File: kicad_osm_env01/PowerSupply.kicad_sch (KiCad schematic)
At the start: 27 parts, among them J5 USB_C_Receptacle_USB2.0, U1 LM66100DCKR, U4 LM66100DCKR, U9 TLV1117LV33DCYR

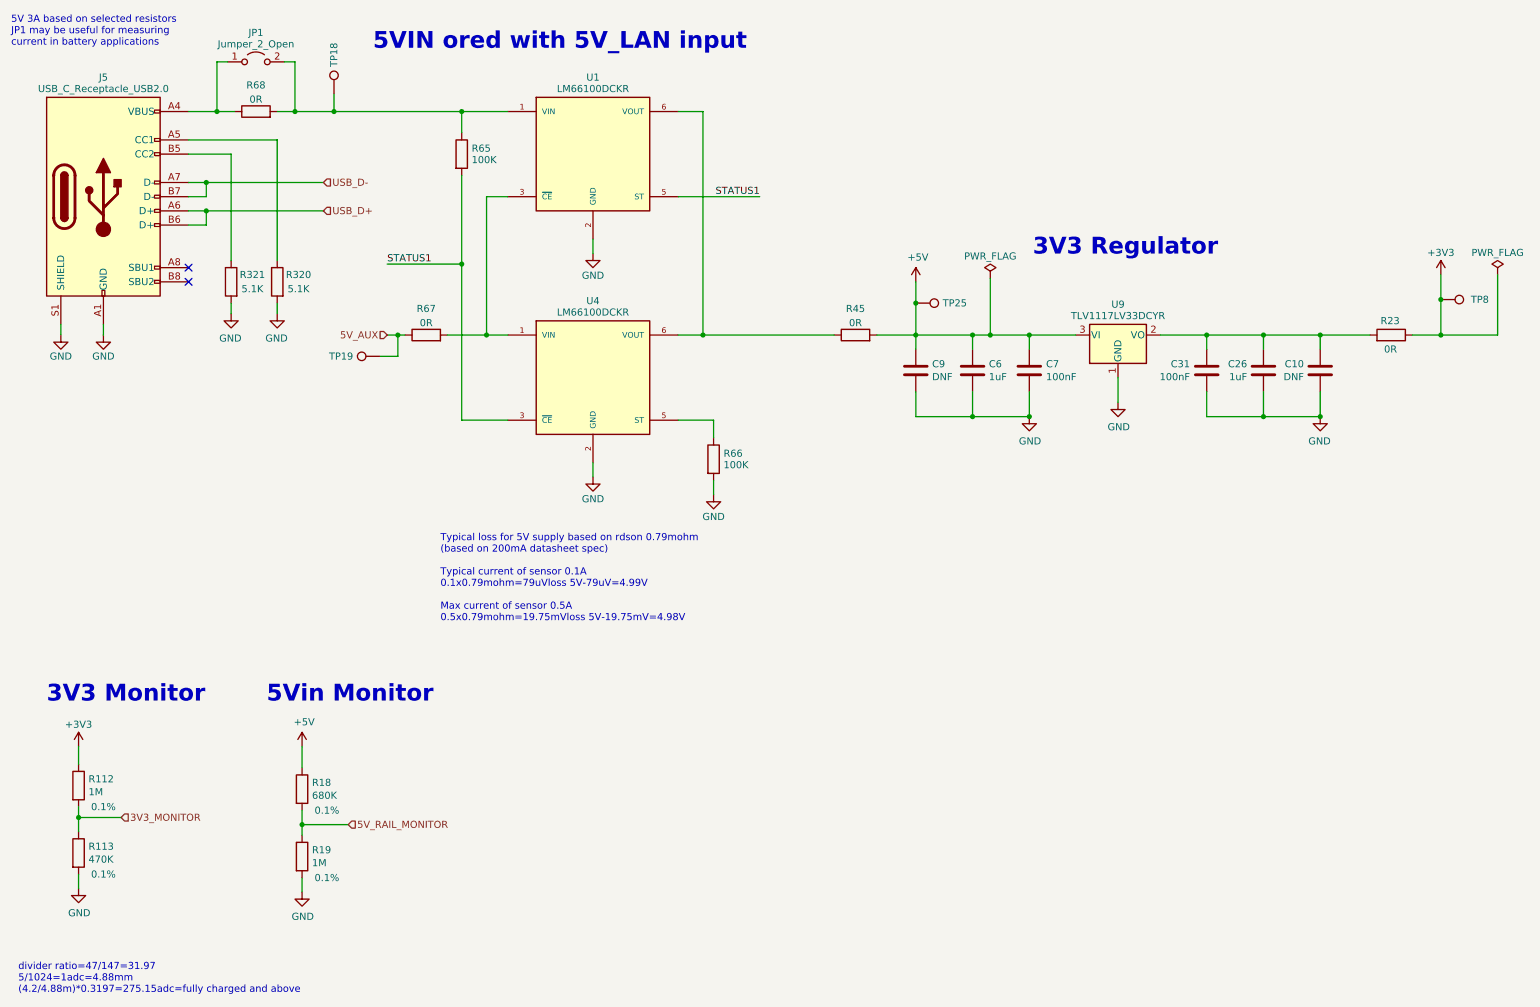
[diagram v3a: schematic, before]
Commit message: updated schematics
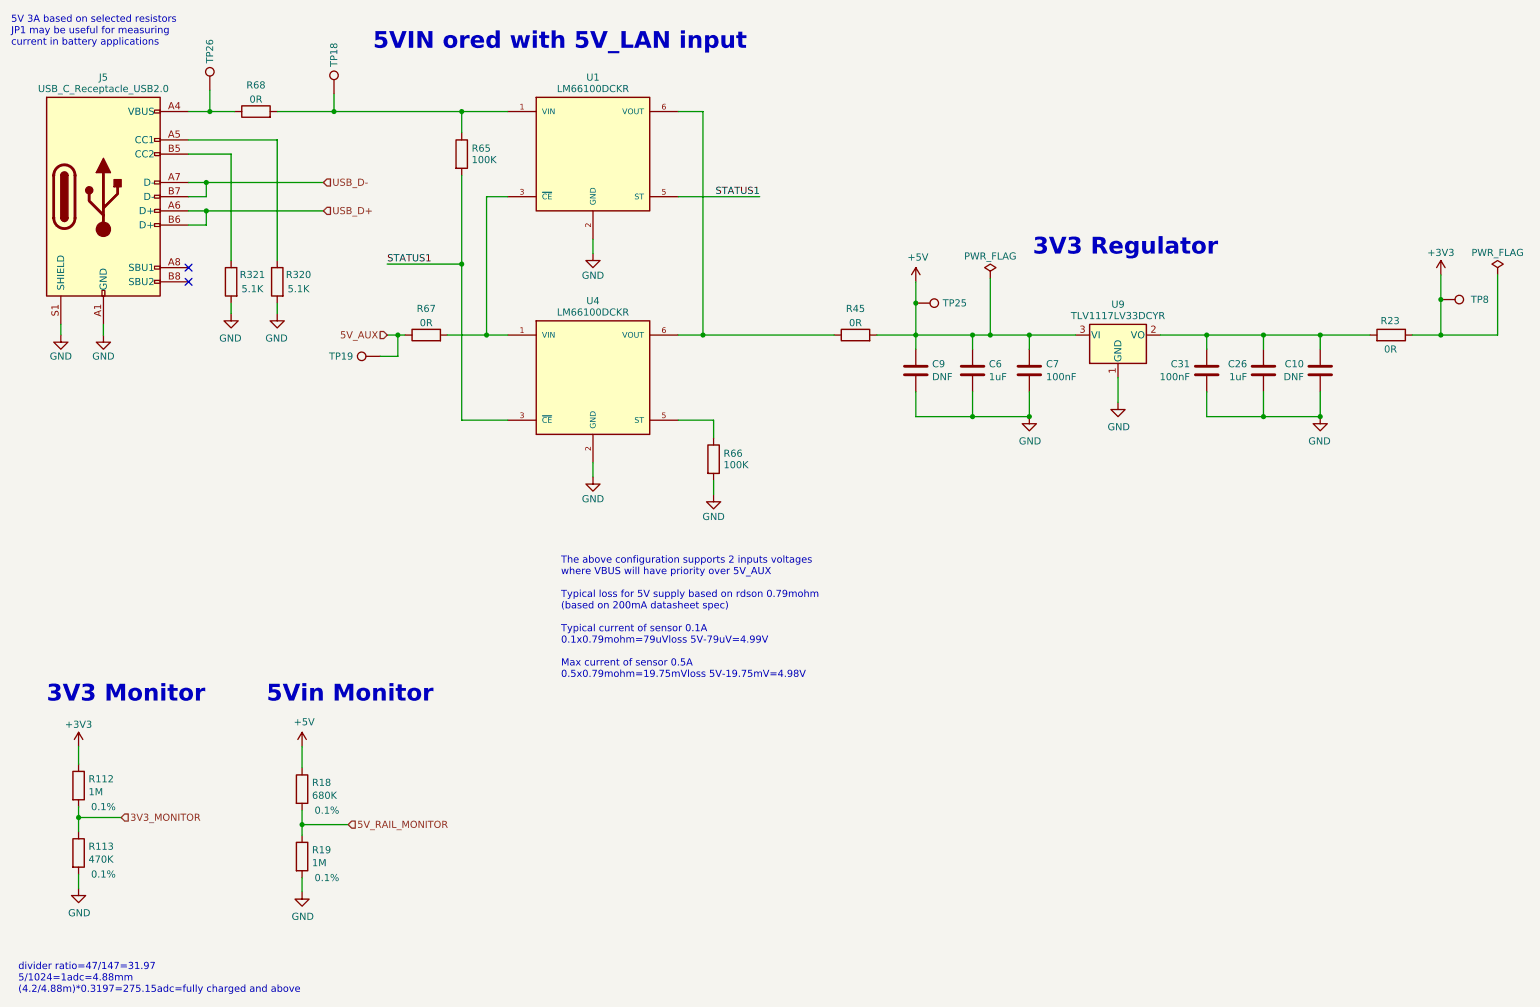
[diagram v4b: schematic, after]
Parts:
- removed JP1: Jumper_2_Open, Connector_PinSocket_2.54mm:PinSocket_1x02_P2.54mm_Vertical, symbol Jumper:Jumper_2_Open
- added TP26: Test_Point, TestPoint:TestPoint_THTPad_D1.0mm_Drill0.5mm, symbol OSM_env01-rescue:Test_Point-Connector-ESP32-EVB_Rev_D-rescue
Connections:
- net at J5.A4 (VBUS), J5.A9 (VBUS), J5.B4 (VBUS)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: now also TP26.1
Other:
- note added: "The above configuration supports 2 inputs voltages where VBUS will have priority over 5V_AUX Typical loss for 5V supply based on rdson 0.79mohm (based on 200mA datasheet spec) Typical current of sensor 0.1A 0.1x0.79mohm=79uVloss 5V-79uV=4.99V Max current of sensor 0.5A 0.5x0.79mohm=19.75mVloss 5V-19.75mV=4.98V"
- note removed: "Typical loss for 5V supply based on rdson 0.79mohm (based on 200mA datasheet spec) Typical current of sensor 0.1A 0.1x0.79mohm=79uVloss 5V-79uV=4.99V Max current of sensor 0.5A 0.5x0.79mohm=19.75mVloss 5V-19.75mV=4.98V"
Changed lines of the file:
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@@
   (junction (at 196.215 90.17) (diameter 0) (color 0 0 0 0)
   )
+  (junction (at 49.53 35.56) (diameter 0) (color 0 0 0 0)
+  )
   (junction (at 269.875 75.565) (diameter 0) (color 0 0 0 0)
   )
@@
   (junction (at 83.185 75.565) (diameter 0) (color 0 0 0 0)
   )
-  (junction (at 50.8 35.56) (diameter 0) (color 0 0 0 0)
-  )
   (junction (at 227.965 75.565) (diameter 0) (color 0 0 0 0)
   )
@@
   )
   (junction (at 137.795 75.565) (diameter 0) (color 0 0 0 0)
-  )
-  (junction (at 64.77 35.56) (diameter 0) (color 0 0 0 0)
   )
   (junction (at 175.895 75.565) (diameter 0) (color 0 0 0 0)
@@
     (stroke (width 0) (type default))
   )
-  (wire (pts (xy 50.8 35.56) (xy 53.975 35.56))
-    (stroke (width 0) (type default))
-  )
   (wire (pts (xy 219.71 75.565) (xy 227.965 75.565))
     (stroke (width 0) (type default))
@@
     (stroke (width 0) (type default))
   )
-  (wire (pts (xy 50.8 26.67) (xy 50.8 35.56))
+  (wire (pts (xy 49.53 35.56) (xy 53.975 35.56))
     (stroke (width 0) (type default))
   )
@@
     (stroke (width 0) (type default))
   )
-  (wire (pts (xy 62.865 26.67) (xy 64.77 26.67))
-    (stroke (width 0) (type default))
-  )
   (wire (pts (xy 102.87 50.8) (xy 99.06 50.8))
     (stroke (width 0) (type default))
@@
     (stroke (width 0) (type default))
   )
+  (wire (pts (xy 49.53 31.75) (xy 49.53 35.56))
+    (stroke (width 0) (type default))
+  )
   (wire (pts (xy 212.09 83.185) (xy 212.09 87.63))
     (stroke (width 0) (type default))
@@
     (stroke (width 0) (type default))
   )
-  (wire (pts (xy 61.595 35.56) (xy 64.77 35.56))
+  (wire (pts (xy 61.595 35.56) (xy 71.755 35.56))
     (stroke (width 0) (type default))
   )
@@
     (stroke (width 0) (type default))
   )
-  (wire (pts (xy 52.705 26.67) (xy 50.8 26.67))
-    (stroke (width 0) (type default))
-  )
   (wire (pts (xy 48.895 48.26) (xy 45.72 48.26))
     (stroke (width 0) (type default))
@@
     (stroke (width 0) (type default))
   )
-  (wire (pts (xy 64.77 35.56) (xy 71.755 35.56))
-    (stroke (width 0) (type default))
-  )
   (wire (pts (xy 189.23 75.565) (xy 196.215 75.565))
     (stroke (width 0) (type default))
@@
     (stroke (width 0) (type default))
   )
-  (wire (pts (xy 45.72 35.56) (xy 50.8 35.56))
+  (wire (pts (xy 45.72 35.56) (xy 49.53 35.56))
     (stroke (width 0) (type default))
   )
@@
   )
   (wire (pts (xy 26.035 149.225) (xy 26.035 152.4))
-    (stroke (width 0) (type default))
-  )
-  (wire (pts (xy 64.77 26.67) (xy 64.77 35.56))
     (stroke (width 0) (type default))
   )
@@
     (effects (font (size 2.9972 2.9972) (thickness 0.5994) bold) (justify left bottom))
   )
-  (text "Typical loss for 5V supply based on rdson 0.79mohm\n(based on 200mA datasheet spec)\n\nTypical current of sensor 0.1A\n0.1x0.79mohm=79uVloss 5V-79uV=4.99V\n\nMax current of sensor 0.5A\n0.5x0.79mohm=19.75mVloss 5V-19.75mV=4.98V"
-    (at 90.805 127 0)
+  (text "The above configuration supports 2 inputs voltages\nwhere VBUS will have priority over 5V_AUX\n\nTypical loss for 5V supply based on rdson 0.79mohm\n(based on 200mA datasheet spec)\n\nTypical current of sensor 0.1A\n0.1x0.79mohm=79uVloss 5V-79uV=4.99V\n\nMax current of sensor 0.5A\n0.5x0.79mohm=19.75mVloss 5V-19.75mV=4.98V"
+    (at 112.395 137.16 0)
     (effects (font (size 1.27 1.27)) (justify left bottom))
   )
@@
         (path "/ab8b0540-9c9f-4195-88f5-7bed0b0a8ed6/00000000-0000-0000-0000-000060688d25"
           (reference "#PWR046") (unit 1)
-        )
-      )
-    )
-  )
-  (symbol (lib_id "Jumper:Jumper_2_Open") (at 57.785 26.67 0) (unit 1)
-    (in_bom yes) (on_board yes) (dnp no) (fields_autoplaced)
-    (property "Reference" "JP1" (at 57.785 21.439 0)
-      (effects (font (size 1.27 1.27)))
-    )
-    (property "Value" "Jumper_2_Open" (at 57.785 23.487 0)
-      (effects (font (size 1.27 1.27)))
-    )
-    (property "Footprint" "Connector_PinSocket_2.54mm:PinSocket_1x02_P2.54mm_Vertical" (at 57.785 26.67 0)
-      (effects (font (size 1.27 1.27)) hide)
-    )
-    (property "Datasheet" "~" (at 57.785 26.67 0)
-      (effects (font (size 1.27 1.27)) hide)
-    )
-    (pin "1")
-    (pin "2")
-    (instances
-      (project "OSM_env01"
-        (path "/ab8b0540-9c9f-4195-88f5-7bed0b0a8ed6/00000000-0000-0000-0000-000060688d25"
-          (reference "JP1") (unit 1)
         )
       )
@@
         )
       )
+    )
+  )
+  (symbol (lib_id "OSM_env01-rescue:Test_Point-Connector-ESP32-EVB_Rev_D-rescue") (at 49.53 31.75 0) (unit 1)
+    (in_bom yes) (on_board yes) (dnp no)
+    (property "Reference" "TP26" (at 49.53 24.765 90)
+      (effects (font (size 1.27 1.27)))
+    )
+    (property "Value" "Test_Point" (at 50.165 35.56 0)
+      (effects (font (size 1.27 1.27)) hide)
+    )
+    (property "Footprint" "TestPoint:TestPoint_THTPad_D1.0mm_Drill0.5mm" (at 54.61 31.75 0)
+      (effects (font (size 1.27 1.27)) hide)
+    )
+    (property "Datasheet" "~" (at 54.61 31.75 0)
+      (effects (font (size 1.27 1.27)) hide)
+    )
+    (pin "1")
+    (instances
+      (project "OSM_env01"
+        (path "/ab8b0540-9c9f-4195-88f5-7bed0b0a8ed6/00000000-0000-0000-0000-000060688d25"
+          (reference "TP26") (unit 1)
+        )
+      )

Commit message: added tracking to layout
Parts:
- TP18, TP19, TP25, TP26, TP8: footprint TestPoint:TestPoint_THTPad_D1.0mm_Drill0.5mm -> TestPoint:TestPoint_Pad_D1.5mm
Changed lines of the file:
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@@
       (effects (font (size 1.27 1.27)) hide)
     )
-    (property "Footprint" "TestPoint:TestPoint_THTPad_D1.0mm_Drill0.5mm" (at 175.895 74.93 0)
+    (property "Footprint" "TestPoint:TestPoint_Pad_D1.5mm" (at 175.895 74.93 0)
       (effects (font (size 1.27 1.27)) hide)
     )
@@
       (effects (font (size 1.27 1.27)) hide)
     )
-    (property "Footprint" "TestPoint:TestPoint_THTPad_D1.0mm_Drill0.5mm" (at 80.01 74.295 0)
+    (property "Footprint" "TestPoint:TestPoint_Pad_D1.5mm" (at 80.01 74.295 0)
       (effects (font (size 1.27 1.27)) hide)
     )
@@
       (effects (font (size 1.27 1.27)) hide)
     )
-    (property "Footprint" "TestPoint:TestPoint_THTPad_D1.0mm_Drill0.5mm" (at 269.875 74.295 0)
+    (property "Footprint" "TestPoint:TestPoint_Pad_D1.5mm" (at 269.875 74.295 0)
       (effects (font (size 1.27 1.27)) hide)
     )
@@
       (effects (font (size 1.27 1.27)) hide)
     )
-    (property "Footprint" "TestPoint:TestPoint_THTPad_D1.0mm_Drill0.5mm" (at 76.835 32.385 0)
+    (property "Footprint" "TestPoint:TestPoint_Pad_D1.5mm" (at 76.835 32.385 0)
       (effects (font (size 1.27 1.27)) hide)
     )
@@
       (effects (font (size 1.27 1.27)) hide)
     )
-    (property "Footprint" "TestPoint:TestPoint_THTPad_D1.0mm_Drill0.5mm" (at 54.61 31.75 0)
-      (effects (font (size 1.27 1.27)) hide)
-    )
+    (property "Footprint" "TestPoint:TestPoint_Pad_D1.5mm" (at 54.61 31.75 0)
+      (effects (font (size 1.27 1.27)) hide)
+    )
